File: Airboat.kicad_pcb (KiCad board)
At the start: 2 copper layers, 7.5 x 2 mm, 47 parts, among them J1 USB_B_Micro, J2 Barrel_Jack_Switch_Pin3Ring, J3 Screw_Terminal_01x02, J5 Screw_Terminal_01x02, Q1 BC847, Q2 BC847, SW1 SW_Omron_B3FS, SW3 SW_Omron_B3FS, U1 ESP32-WROOM-32E, U2 CP2102N-Axx-xQFN28, U3 AP2127N-3.3, U4 AP2204RB-5.0, U5 L293D, X1 SG-3030CM

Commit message: Started to layout PCB
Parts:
- added H1: MountingHole, MountingHole:MountingHole_2.2mm_M2, F.Cu at (105.0, 55.0)
- added H2: MountingHole, MountingHole:MountingHole_2.2mm_M2, F.Cu at (195.0, 55.0)
- added H3: MountingHole, MountingHole:MountingHole_2.2mm_M2, F.Cu at (105.0, 145.0)
- added H5: MountingHole, MountingHole:MountingHole_2.2mm_M2, F.Cu at (195.0, 145.0)
- moved U4 126.8 mm to (10.8, 90.5)
- moved C4 126.8 mm to (1.20, 124.1)
- moved C5 126.8 mm to (5.25, 76.4)
- moved C6 126.8 mm to (5.25, 78.9)
- moved C7 126.8 mm to (5.25, 81.4)
- moved C8 126.8 mm to (5.25, 83.9)
- moved D1 126.8 mm to (5.20, 124.0)
- moved D2 126.8 mm to (5.20, 126.5)
- moved D3 126.8 mm to (5.20, 128.9)
- moved D4 126.8 mm to (5.20, 131.4)
- moved D5 126.8 mm to (20.2, 88.6)
- moved D6 126.8 mm to (20.2, 91.1)
- moved D7 126.8 mm to (16.0, 88.9)
- moved D8 126.8 mm to (16.0, 92.0)
- moved Q1 126.8 mm to (9.09, 124.8)
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- renumbered Q2 to Q3
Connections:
- C1 pad 1: MCU_EN -> EN
- Q3 pad 1: Net-(Q2-B) -> Net-(Q3-B)
- R1 pad 2: MCU_EN -> EN
- R6 pad 2: Net-(Q2-B) -> Net-(Q3-B)
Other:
- board size 7.5 x 2 mm -> 100 x 100 mm

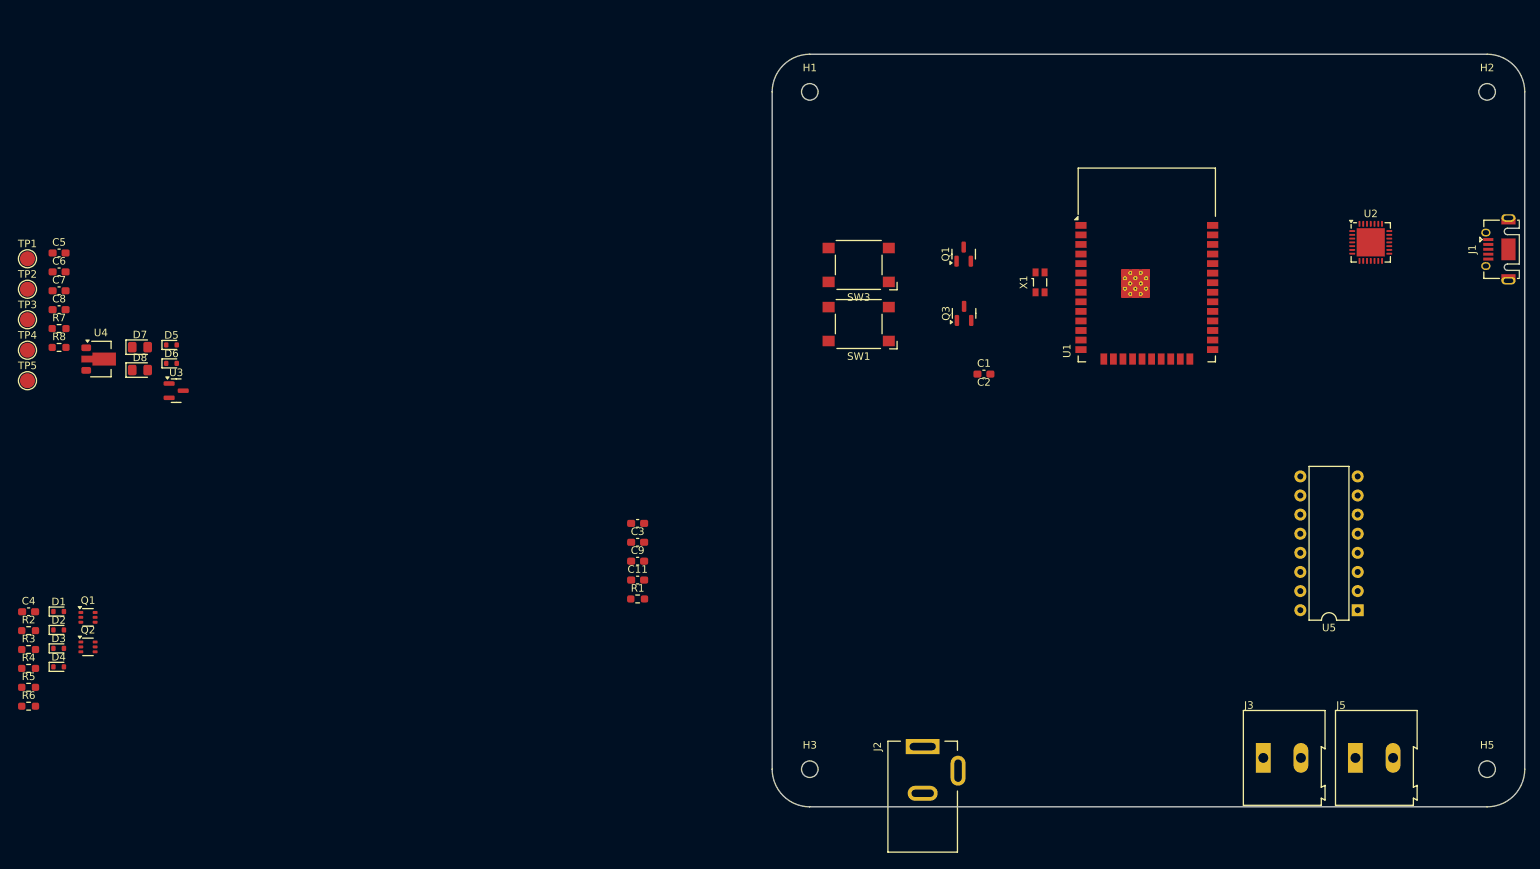
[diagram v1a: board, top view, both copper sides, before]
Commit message: Placed all components on PCB
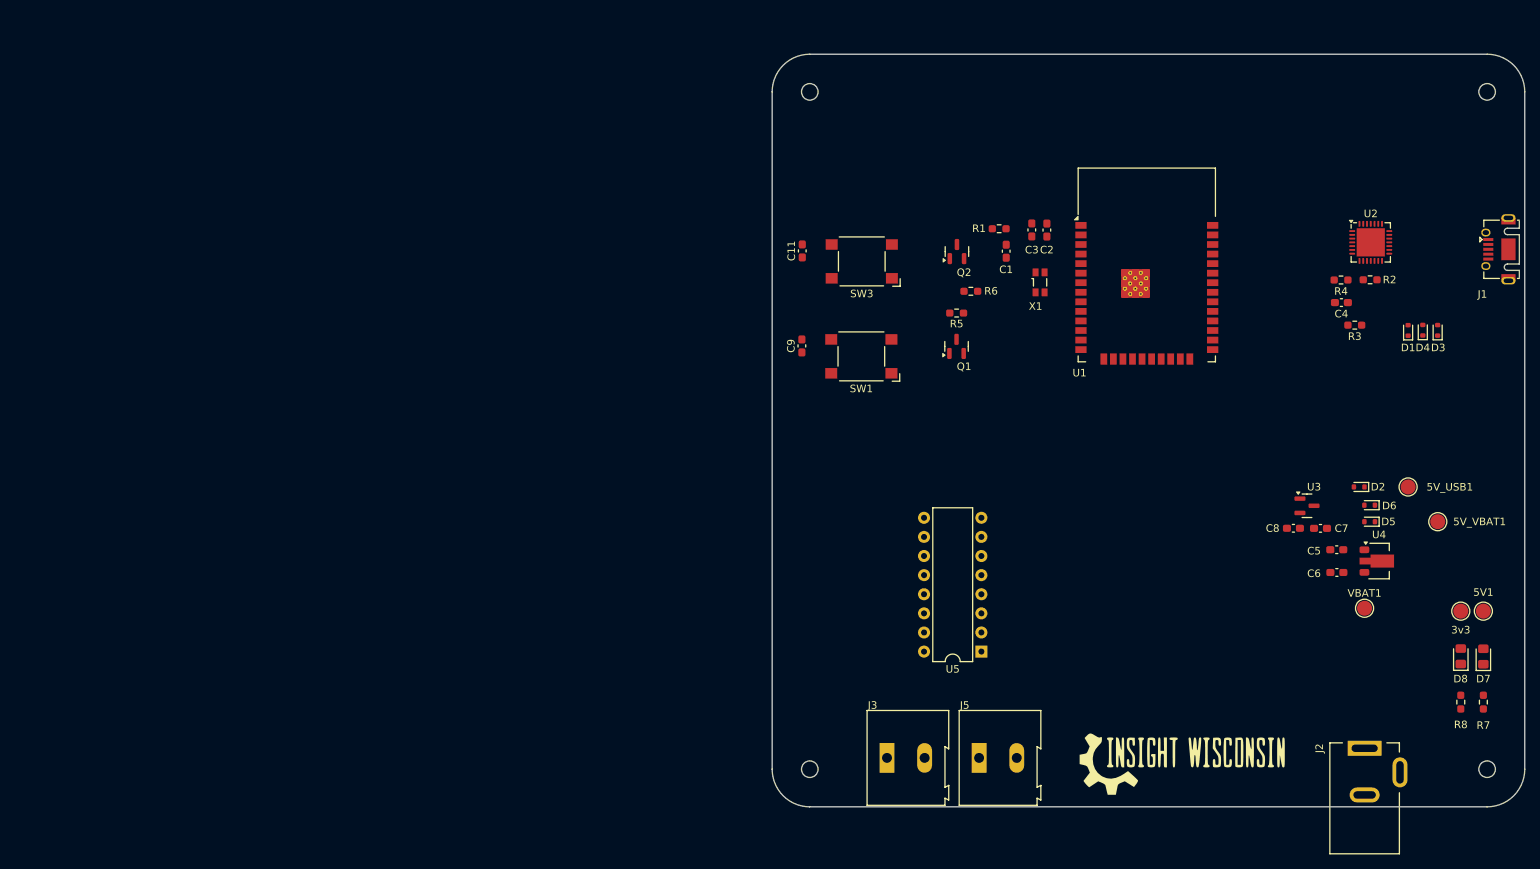
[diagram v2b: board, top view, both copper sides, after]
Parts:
- removed the Q1 at (9.09, 124.8)
- removed the Q1 at (125.5, 76.6)
- removed Q3: BC847, Package_TO_SOT_SMD:SOT-23
- added L1: ~, Insight Logo:Insight_Logo, F.Cu at (155.5, 144.0)
- added Q1: BC818, Package_TO_SOT_SMD:SOT-23, F.Cu at (124.5, 88.8)
- C2: value 1uF -> 22uF
- C3: value 1uF -> 0.1uF
- Q2: value BC847 -> BC818; footprint Package_TO_SOT_SMD:SOT-363_SC-70-6 -> Package_TO_SOT_SMD:SOT-23
- moved 5V1 196.5 mm to (194.5, 124.0)
- moved R7 195.7 mm to (194.5, 136.1), turned to -90 degrees
- moved 3v3 192.9 mm to (191.5, 124.0)
- moved R8 192.1 mm to (191.5, 136.1), turned to -90 degrees
- moved 5V_VBAT1 189.3 mm to (188.4, 112.1)
- moved D3 188.0 mm to (188.4, 86.7), turned to 90 degrees
- moved D4 186.7 mm to (186.5, 86.7), turned to 90 degrees
- moved 5V_USB1 185.3 mm to (184.5, 107.5)
- moved R2 184.2 mm to (179.5, 80.0), turned to 180 degrees
- moved VBAT1 183.6 mm to (178.7, 123.6)
- moved D7 183.2 mm to (194.5, 130.0), turned to 90 degrees
- moved D1 183.2 mm to (184.5, 86.7), turned to 90 degrees
- moved R4 181.9 mm to (175.6, 80.0), turned to 180 degrees
- moved R3 181.4 mm to (177.4, 86.0), turned to 180 degrees
- moved D8 179.6 mm to (191.5, 130.0), turned to 90 degrees
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- renumbered TP5 to 3v3, TP4 to 5V1, TP2 to 5V_USB1, TP3 to 5V_VBAT1, TP1 to VBAT1
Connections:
- net Net-(U2-VBUS) renamed /USB/CP2102_VBUS
- net Net-(U2-~{RST}) renamed /USB/CP2102_RST
- Q2 pad 1: Net-(Q2-B) -> /USB/DTR_BASE
- Q2 pad 2: DTR -> RTS
- Q2 pad 3: IO0 -> EN
- R5 pad 2: Net-(Q1-B) -> /USB/DTR_BASE
- R6 pad 2: Net-(Q3-B) -> /USB/RTS_BASE

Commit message: Removed uneeeded components, started to lay PCB traces
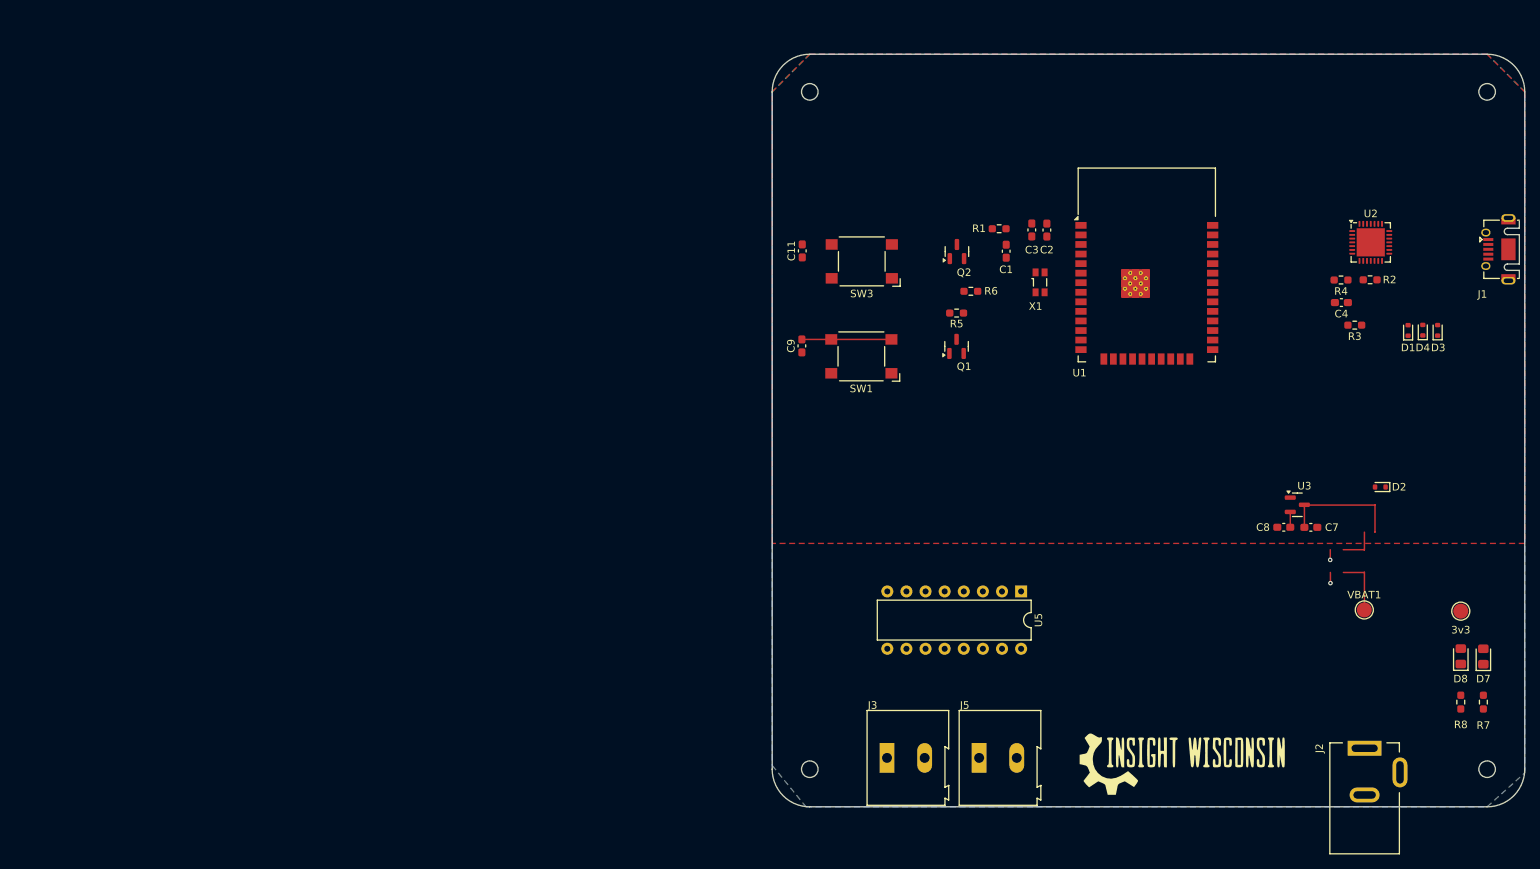
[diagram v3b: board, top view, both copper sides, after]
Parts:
- removed 5V1: 5V_TP, TestPoint:TestPoint_Pad_D2.0mm
- removed 5V_USB1: 5VUSB_TP, TestPoint:TestPoint_Pad_D2.0mm
- removed 5V_VBAT1: 5VBAT_TP, TestPoint:TestPoint_Pad_D2.0mm
- removed C5, C6: 1uF, Capacitor_SMD:C_0603_1608Metric_Pad1.08x0.95mm_HandSolder
- removed D5, D6: D_Schottky_Small, Diode_SMD:D_SOD-523
- removed U4: AP2204RB-5.0, Package_TO_SOT_SMD:SOT-89-3
- moved U5 9.58 mm to (133.1, 121.4), turned to -90 degrees
- moved D2 2.81 mm to (180.8, 107.5)
- moved C7 1.29 mm to (171.6, 112.9)
- moved C8 1.29 mm to (168.0, 112.9)
- moved U3 1.29 mm to (169.8, 109.9)
- moved VBAT1 0.23 mm to (178.7, 123.8)
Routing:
- net +5V: track 0.00 -> 16.0 mm
- net IO0: track 0.00 -> 11.9 mm
- net +BATT: track 0.00 -> 7.80 mm
- net (no net): track 0.00 -> 5.16 mm
- net GND: track 0.00 -> 2.78 mm, vias 0 -> 2
- net +3.3V: track 0.00 -> 2.04 mm
- added copper zone on F.Cu, net +3.3V
- added copper zone on B.Cu, net GND

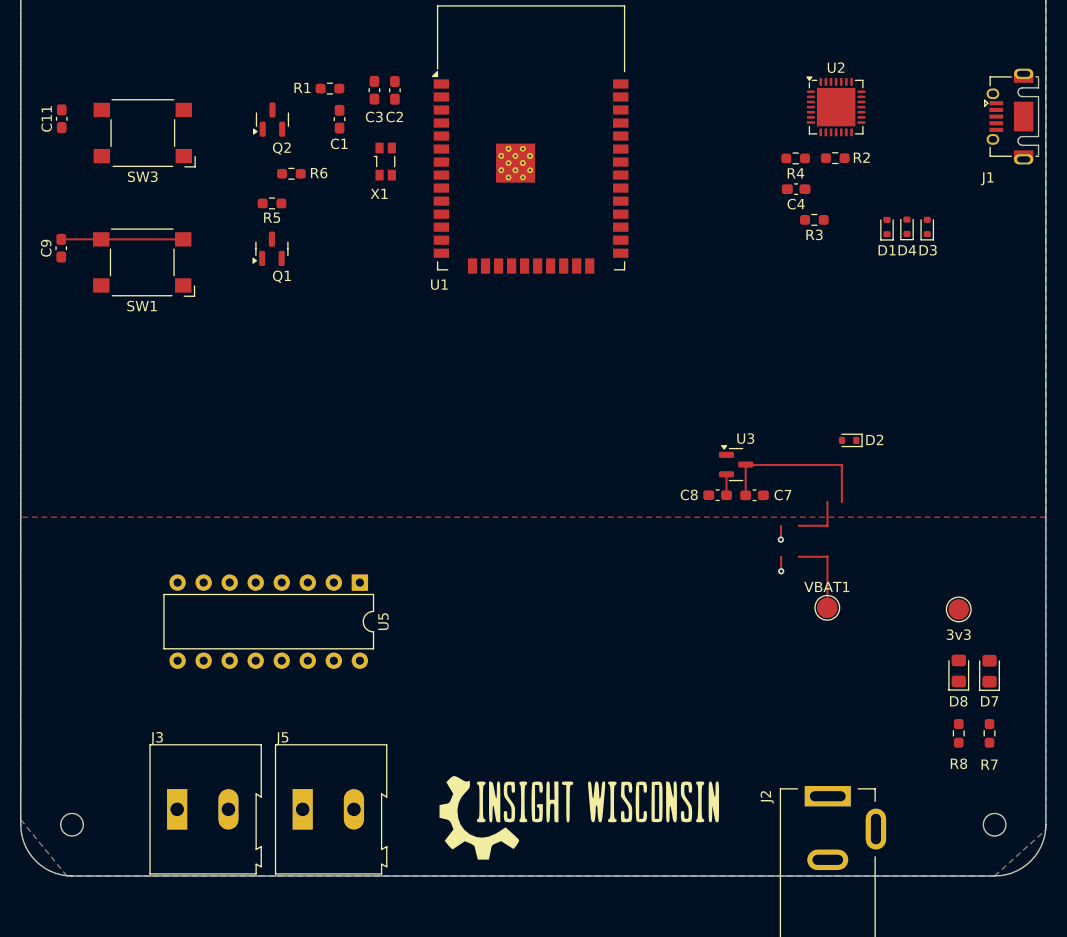
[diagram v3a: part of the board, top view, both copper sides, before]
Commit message: Finished PCB routing
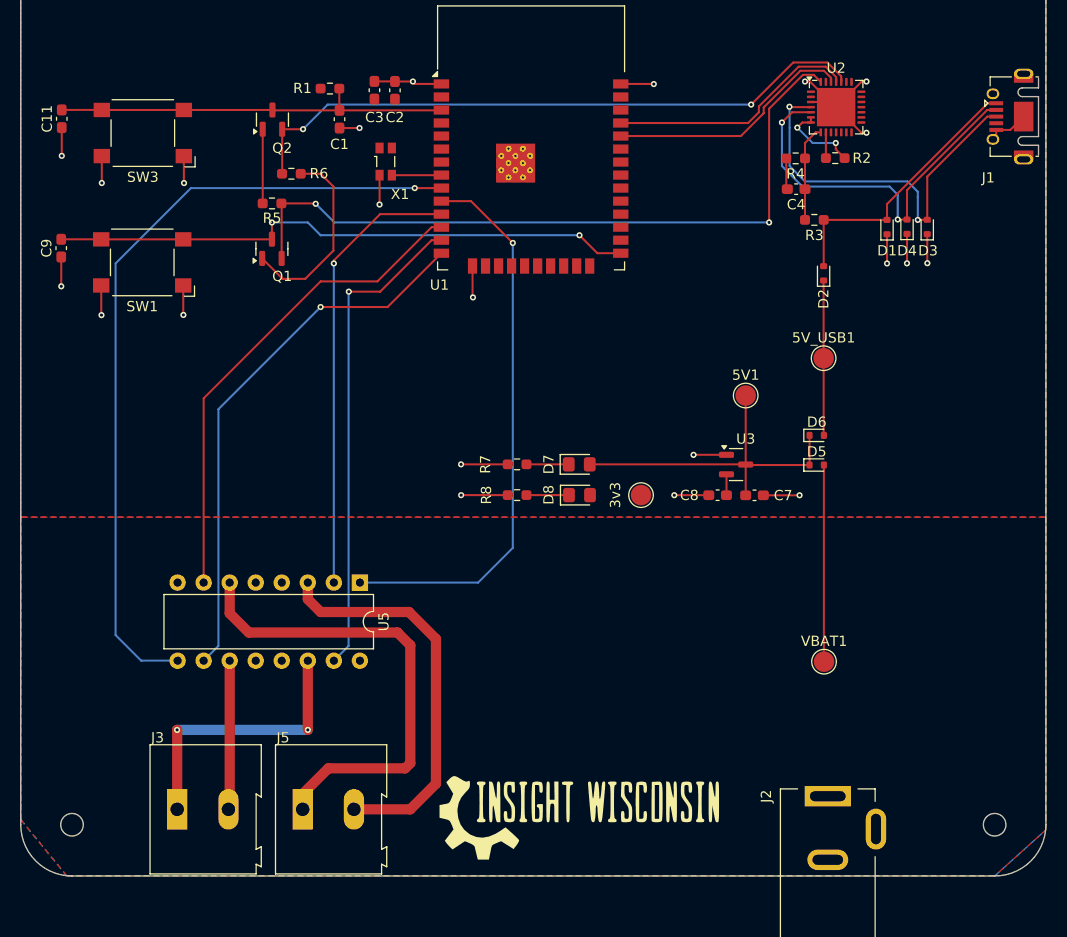
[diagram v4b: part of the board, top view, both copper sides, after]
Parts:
- added 5V1: 5V_TP, TestPoint:TestPoint_Pad_D2.0mm, F.Cu at (170.7, 103.1)
- added 5V_USB1: 5VUSB_TP, TestPoint:TestPoint_Pad_D2.0mm, F.Cu at (178.3, 99.5)
- added D5: D_Schottky_Small, Diode_SMD:D_SOD-523, F.Cu at (177.6, 109.9)
- added D6: D_Schottky_Small, Diode_SMD:D_SOD-523, F.Cu at (177.6, 107.0)
- moved R7 53.0 mm to (148.4, 109.8), turned to 180 degrees
- moved R8 49.0 mm to (148.4, 112.8), turned to 180 degrees
- moved D7 44.8 mm to (154.5, 109.8), turned to 0 degrees
- moved D8 40.8 mm to (154.5, 112.8), turned to 0 degrees
- moved 3v3 32.9 mm to (160.5, 112.8), turned to -90 degrees
- moved D2 16.5 mm to (178.3, 91.2), turned to 90 degrees
- moved VBAT1 5.26 mm to (178.4, 129.1)
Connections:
- net +5V renamed +V_MCU
- U1 pad 10: RUDDER_B -> FAN_PWM
- U1 pad 11: unconnected-(U1-IO26-Pad11) -> FAN_F
- U1 pad 12: unconnected-(U1-IO27-Pad12) -> FAN_B
- U1 pad 13: unconnected-(U1-IO14-Pad13) -> RUDDER_B
- U1 pad 14: unconnected-(U1-IO12-Pad14) -> RUDDER_F
- U1 pad 33: FAN_F -> unconnected-(U1-IO21-Pad33)
- U1 pad 36: FAN_B -> unconnected-(U1-IO22-Pad36)
- U1 pad 37: RUDDER_F -> unconnected-(U1-IO23-Pad37)
- U1 pad 9: unconnected-(U1-IO33-Pad9) -> RUDDER_PWM
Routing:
- net GND: track 2.78 -> 81.2 mm, vias 2 -> 22
- net RUDDER_PWM: track 0.00 -> 78.2 mm, vias 0 -> 1
- net DTR: track 0.00 -> 71.5 mm, vias 0 -> 2
- net RTS: track 0.00 -> 62.7 mm, vias 0 -> 2
- net FAN_PWM: track 0.00 -> 54.7 mm, vias 0 -> 1
- net RUDDER_F: track 0.00 -> 53.2 mm, vias 0 -> 1
- net RUDDER_B: track 0.00 -> 48.4 mm, vias 0 -> 1
- net FAN_B: track 0.00 -> 48.1 mm
- net FAN_NEG: track 0.00 -> 46.7 mm
- net IO0: track 11.9 -> 57.5 mm, vias 0 -> 2
- net FAN_F: track 0.00 -> 43.8 mm, vias 0 -> 1
- net EN: track 0.00 -> 39.2 mm
- net FAN_POS: track 0.00 -> 38.9 mm
- net USB_DP: track 0.00 -> 38.5 mm, vias 0 -> 2
- net USB_DM: track 0.00 -> 38.1 mm, vias 0 -> 2
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- added copper zone on F.Cu, net +BATT
